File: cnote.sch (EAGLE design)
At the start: 9 parts

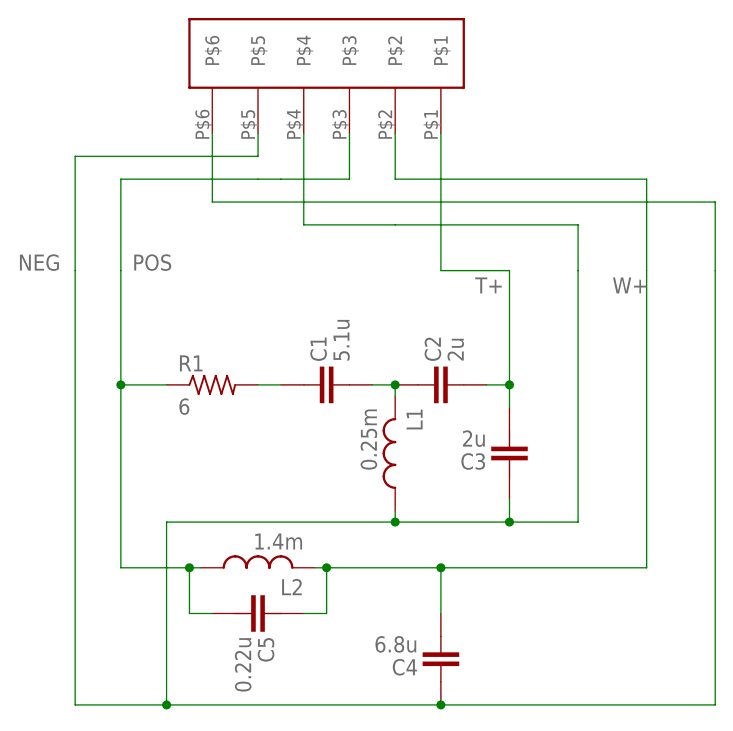
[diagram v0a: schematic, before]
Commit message: Fixed connector part number
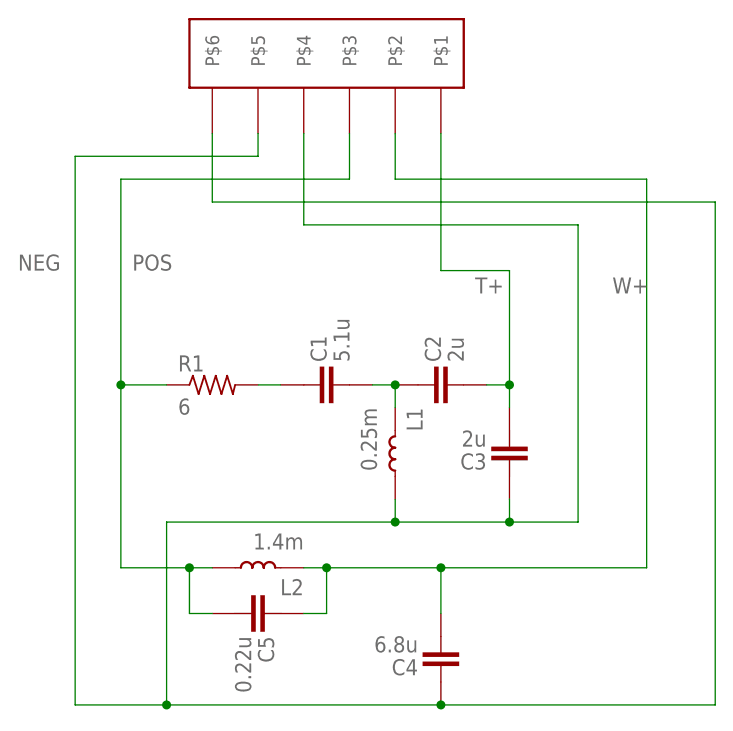
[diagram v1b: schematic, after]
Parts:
- U$1: value WURTH_WR-TBL-2418-6 -> WURTH_WR-TBL-2416-6; device travis:WURTH_WR-TBL-2418-6 -> travis:WURTH_WR-TBL-2416-6
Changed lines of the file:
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@@
 <?xml version="1.0" encoding="utf-8"?>
 <!DOCTYPE eagle SYSTEM "eagle.dtd">
-<eagle version="9.1.3">
+<eagle version="9.2.2">
 <drawing>
 <settings>
@@
 <setting verticaltext="up"/>
 </settings>
-<grid distance="0.05" unitdist="inch" unit="inch" style="lines" multiple="1" display="no" altdistance="0.01" altunitdist="inch" altunit="inch"/>
+<grid distance="0.1" unitdist="inch" unit="inch" style="lines" multiple="1" display="no" altdistance="0.01" altunitdist="inch" altunit="inch"/>
 <layers>
 <layer number="1" name="Top" color="4" fill="1" visible="no" active="no"/>
@@
 <part name="L2" library="travis" deviceset="DAYTON_AC201-4" device="" value="1.4m"/>
 <part name="C5" library="travis" deviceset="DAYTON_DMPC-0.22" device="" value="0.22u"/>
-<part name="U$1" library="travis" deviceset="WURTH_WR-TBL-2418-6" device=""/>
+<part name="U$1" library="travis" deviceset="WURTH_WR-TBL-2416-6" device=""/>
 </parts>
 <sheets>
@@
 </plain>
 <instances>
-<instance part="R1" gate="G$1" x="38.1" y="55.88"/>
-<instance part="C1" gate="G$1" x="50.8" y="55.88" rot="R90"/>
-<instance part="C2" gate="G$1" x="63.5" y="55.88" rot="R90"/>
-<instance part="C3" gate="G$1" x="71.12" y="48.26" rot="R180"/>
-<instance part="C4" gate="G$1" x="63.5" y="25.4" rot="R180"/>
-<instance part="L1" gate="G$1" x="58.42" y="48.26" rot="R180"/>
-<instance part="L2" gate="G$1" x="43.18" y="35.56" rot="R90"/>
-<instance part="C5" gate="G$1" x="43.18" y="30.48" rot="R270"/>
-<instance part="U$1" gate="G$1" x="50.8" y="88.9" rot="R270"/>
+<instance part="R1" gate="G$1" x="38.1" y="55.88" smashed="yes">
+<attribute name="NAME" x="34.29" y="57.3786" size="1.778" layer="95"/>
+<attribute name="VALUE" x="34.29" y="52.578" size="1.778" layer="96"/>
+</instance>
+<instance part="C1" gate="G$1" x="50.8" y="55.88" smashed="yes" rot="R90">
+<attribute name="NAME" x="50.8" y="58.42" size="1.778" layer="95" rot="R90"/>
+<attribute name="VALUE" x="53.34" y="58.42" size="1.778" layer="96" rot="R90"/>
+</instance>
+<instance part="C2" gate="G$1" x="63.5" y="55.88" smashed="yes" rot="R90">
+<attribute name="NAME" x="63.5" y="58.42" size="1.778" layer="95" rot="R90"/>
+<attribute name="VALUE" x="66.04" y="58.42" size="1.778" layer="96" rot="R90"/>
+</instance>
+<instance part="C3" gate="G$1" x="71.12" y="48.26" smashed="yes" rot="R180">
+<attribute name="NAME" x="68.58" y="48.26" size="1.778" layer="95" rot="R180"/>
+<attribute name="VALUE" x="68.58" y="50.8" size="1.778" layer="96" rot="R180"/>
+</instance>
+<instance part="C4" gate="G$1" x="63.5" y="25.4" smashed="yes" rot="R180">
+<attribute name="NAME" x="60.96" y="25.4" size="1.778" layer="95" rot="R180"/>
+<attribute name="VALUE" x="60.96" y="27.94" size="1.778" layer="96" rot="R180"/>
+</instance>
+<instance part="L1" gate="G$1" x="58.42" y="48.26" smashed="yes" rot="R180">
+<attribute name="NAME" x="59.69" y="53.34" size="1.778" layer="95" rot="R270"/>
+<attribute name="VALUE" x="54.61" y="53.34" size="1.778" layer="96" rot="R270"/>
+</instance>
+<instance part="L2" gate="G$1" x="43.18" y="35.56" smashed="yes" rot="R90">
+<attribute name="NAME" x="48.26" y="34.29" size="1.778" layer="95" rot="R180"/>
+<attribute name="VALUE" x="48.26" y="39.37" size="1.778" layer="96" rot="R180"/>
+</instance>
+<instance part="C5" gate="G$1" x="43.18" y="30.48" smashed="yes" rot="R270">
+<attribute name="NAME" x="43.18" y="27.94" size="1.778" layer="95" rot="R270"/>
+<attribute name="VALUE" x="40.64" y="27.94" size="1.778" layer="96" rot="R270"/>
+</instance>
+<instance part="U$1" gate="G$1" x="50.8" y="88.9" smashed="yes" rot="R270"/>
 </instances>
 <busses>
@@
 <pinref part="L1" gate="G$1" pin="2"/>
 <pinref part="C1" gate="G$1" pin="2"/>
-<wire x1="58.42" y1="54.61" x2="58.42" y2="55.88" width="0.1524" layer="91"/>
+<wire x1="58.42" y1="53.34" x2="58.42" y2="55.88" width="0.1524" layer="91"/>
 <wire x1="58.42" y1="55.88" x2="55.88" y2="55.88" width="0.1524" layer="91"/>
 <junction x="58.42" y="55.88"/>
@@
 <segment>
 <pinref part="L2" gate="G$1" pin="2"/>
-<wire x1="49.53" y1="35.56" x2="50.8" y2="35.56" width="0.1524" layer="91"/>
+<wire x1="48.26" y1="35.56" x2="50.8" y2="35.56" width="0.1524" layer="91"/>
 <wire x1="50.8" y1="35.56" x2="63.5" y2="35.56" width="0.1524" layer="91"/>
 <wire x1="63.5" y1="35.56" x2="86.36" y2="35.56" width="0.1524" layer="91"/>
-<wire x1="86.36" y1="35.56" x2="86.36" y2="68.58" width="0.1524" layer="91"/>
+<wire x1="86.36" y1="35.56" x2="86.36" y2="78.74" width="0.1524" layer="91"/>
 <pinref part="C5" gate="G$1" pin="1"/>
 <wire x1="48.26" y1="30.48" x2="50.8" y2="30.48" width="0.1524" layer="91"/>
@@
 <junction x="63.5" y="35.56"/>
 <label x="82.55" y="66.04" size="1.778" layer="95"/>
-<wire x1="86.36" y1="68.58" x2="86.36" y2="78.74" width="0.1524" layer="91"/>
 <wire x1="86.36" y1="78.74" x2="58.42" y2="78.74" width="0.1524" layer="91"/>
 <pinref part="U$1" gate="G$1" pin="P$2"/>
@@
 <pinref part="L2" gate="G$1" pin="1"/>
 <wire x1="38.1" y1="30.48" x2="35.56" y2="30.48" width="0.1524" layer="91"/>
-<wire x1="36.83" y1="35.56" x2="35.56" y2="35.56" width="0.1524" layer="91"/>
+<wire x1="38.1" y1="35.56" x2="35.56" y2="35.56" width="0.1524" layer="91"/>
 <wire x1="35.56" y1="35.56" x2="27.94" y2="35.56" width="0.1524" layer="91"/>
 <wire x1="27.94" y1="35.56" x2="27.94" y2="55.88" width="0.1524" layer="91"/>
@@
 <wire x1="27.94" y1="55.88" x2="33.02" y2="55.88" width="0.1524" layer="91"/>
 <junction x="27.94" y="55.88"/>
-<wire x1="27.94" y1="55.88" x2="27.94" y2="68.58" width="0.1524" layer="91"/>
+<wire x1="27.94" y1="55.88" x2="27.94" y2="78.74" width="0.1524" layer="91"/>
 <label x="29.21" y="68.58" size="1.778" layer="95"/>
-<wire x1="27.94" y1="68.58" x2="27.94" y2="78.74" width="0.1524" layer="91"/>
-<wire x1="27.94" y1="78.74" x2="43.18" y2="78.74" width="0.1524" layer="91"/>
-<wire x1="43.18" y1="78.74" x2="45.72" y2="78.74" width="0.1524" layer="91"/>
-<wire x1="45.72" y1="78.74" x2="53.34" y2="78.74" width="0.1524" layer="91"/>
+<wire x1="27.94" y1="78.74" x2="53.34" y2="78.74" width="0.1524" layer="91"/>
 <pinref part="U$1" gate="G$1" pin="P$3"/>
 <wire x1="53.34" y1="78.74" x2="53.34" y2="83.82" width="0.1524" layer="91"/>
@@
 <wire x1="63.5" y1="20.32" x2="93.98" y2="20.32" width="0.1524" layer="91"/>
 <junction x="63.5" y="20.32"/>
-<wire x1="93.98" y1="20.32" x2="93.98" y2="68.58" width="0.1524" layer="91"/>
+<wire x1="93.98" y1="20.32" x2="93.98" y2="76.2" width="0.1524" layer="91"/>
 <pinref part="C3" gate="G$1" pin="1"/>
 <pinref part="L1" gate="G$1" pin="1"/>
 <wire x1="71.12" y1="43.18" x2="71.12" y2="40.64" width="0.1524" layer="91"/>
 <wire x1="71.12" y1="40.64" x2="78.74" y2="40.64" width="0.1524" layer="91"/>
-<wire x1="78.74" y1="40.64" x2="78.74" y2="68.58" width="0.1524" layer="91"/>
+<wire x1="78.74" y1="40.64" x2="78.74" y2="73.66" width="0.1524" layer="91"/>
 <junction x="71.12" y="40.64"/>
 <wire x1="33.02" y1="20.32" x2="33.02" y2="40.64" width="0.1524" layer="91"/>
 <wire x1="33.02" y1="20.32" x2="22.86" y2="20.32" width="0.1524" layer="91"/>
-<wire x1="22.86" y1="20.32" x2="22.86" y2="68.58" width="0.1524" layer="91"/>
+<wire x1="22.86" y1="20.32" x2="22.86" y2="81.28" width="0.1524" layer="91"/>
 <junction x="33.02" y="20.32"/>
 <label x="16.51" y="68.58" size="1.778" layer="95"/>
-<wire x1="78.74" y1="68.58" x2="78.74" y2="73.66" width="0.1524" layer="91"/>
-<wire x1="78.74" y1="73.66" x2="58.42" y2="73.66" width="0.1524" layer="91"/>
-<wire x1="93.98" y1="68.58" x2="93.98" y2="76.2" width="0.1524" layer="91"/>
-<wire x1="22.86" y1="68.58" x2="22.86" y2="81.28" width="0.1524" layer="91"/>
+<wire x1="78.74" y1="73.66" x2="48.26" y2="73.66" width="0.1524" layer="91"/>
 <wire x1="22.86" y1="81.28" x2="43.18" y2="81.28" width="0.1524" layer="91"/>
 <pinref part="U$1" gate="G$1" pin="P$5"/>
@@
 <wire x1="38.1" y1="76.2" x2="38.1" y2="83.82" width="0.1524" layer="91"/>
 <pinref part="U$1" gate="G$1" pin="P$4"/>
-<wire x1="58.42" y1="73.66" x2="48.26" y2="73.66" width="0.1524" layer="91"/>
 <wire x1="48.26" y1="73.66" x2="48.26" y2="83.82" width="0.1524" layer="91"/>
 <wire x1="71.12" y1="40.64" x2="58.42" y2="40.64" width="0.1524" layer="91"/>
 <wire x1="58.42" y1="40.64" x2="33.02" y2="40.64" width="0.1524" layer="91"/>
-<wire x1="58.42" y1="41.91" x2="58.42" y2="40.64" width="0.1524" layer="91"/>
+<wire x1="58.42" y1="43.18" x2="58.42" y2="40.64" width="0.1524" layer="91"/>
 <junction x="58.42" y="40.64"/>
 </segment>
